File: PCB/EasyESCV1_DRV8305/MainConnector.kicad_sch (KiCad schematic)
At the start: 3 parts, among them J1 10159560-A00221RLF, J2 TC2050-IDC, U4 LMR16006XDDCR

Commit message: Finished REV1 Schematic Awaiting Review
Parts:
- removed J2: TC2050-IDC, Connector:Tag-Connect_TC2050-IDC-NL_2x05_P1.27mm_Vertical, symbol Connectors:TC2050-IDC
- added 3V3: TestPoint, symbol Connector:TestPoint
- added C18: 390U, symbol Device:C_Polarized_US
- added C19: 0.1U, symbol Device:C
- added C20: 0.33u, symbol Device:C
- added C21: 22u, symbol Device:C
- added C22: 1u, symbol Device:C
- added D2: D_Schottky, symbol Device:D_Schottky
- added L1: 15u, symbol Device:L
- added R13: 24.9K, symbol Device:R_US
- added R14: 4.99K, symbol Device:R_US
- added R15: 68k, symbol Device:R_US
- added R16: 20k, symbol Device:R_US
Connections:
- net PVDD: now reaches J1.1
- net PVDD: now also J1.2, U4.5 (VIN), C18.1, C22.1, R13.1
- net COM: now reaches J1.10
- net GND: now reaches J1.3
- net GND: now also J1.4, J1.8, J1.9, J1.S1 (SHIELD), J1.S2 (SHIELD__1), U4.2 (GND), C18.2, C19.2, C21.2, C22.2, D2.2 (A), R14.2, R16.2
- net MOT_A: now reaches J1.5
- net MOT_B: now reaches J1.6
- net MOT_C: now reaches J1.7
- net at U4.1 (CB): now also C20.2
- net at U4.3 (FB): now also R15.2, R16.1
- net at U4.6 (SW): now also C20.1, D2.1 (K), L1.1
- new net 3.3V: 3V3.1, C21.1, L1.2, R15.1
- new net VSEN_PVDD: C19.1, R13.2, R14.1
- no-connect marks 0 -> 1
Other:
- note added: "3V3 Buck Regulator"
- note added: "Input Power"
- note added: "Main Connector"
- company: (none) -> Buckley Boards 
- title: (none) -> Easy ESC
- moved on the sheet: J1, U4

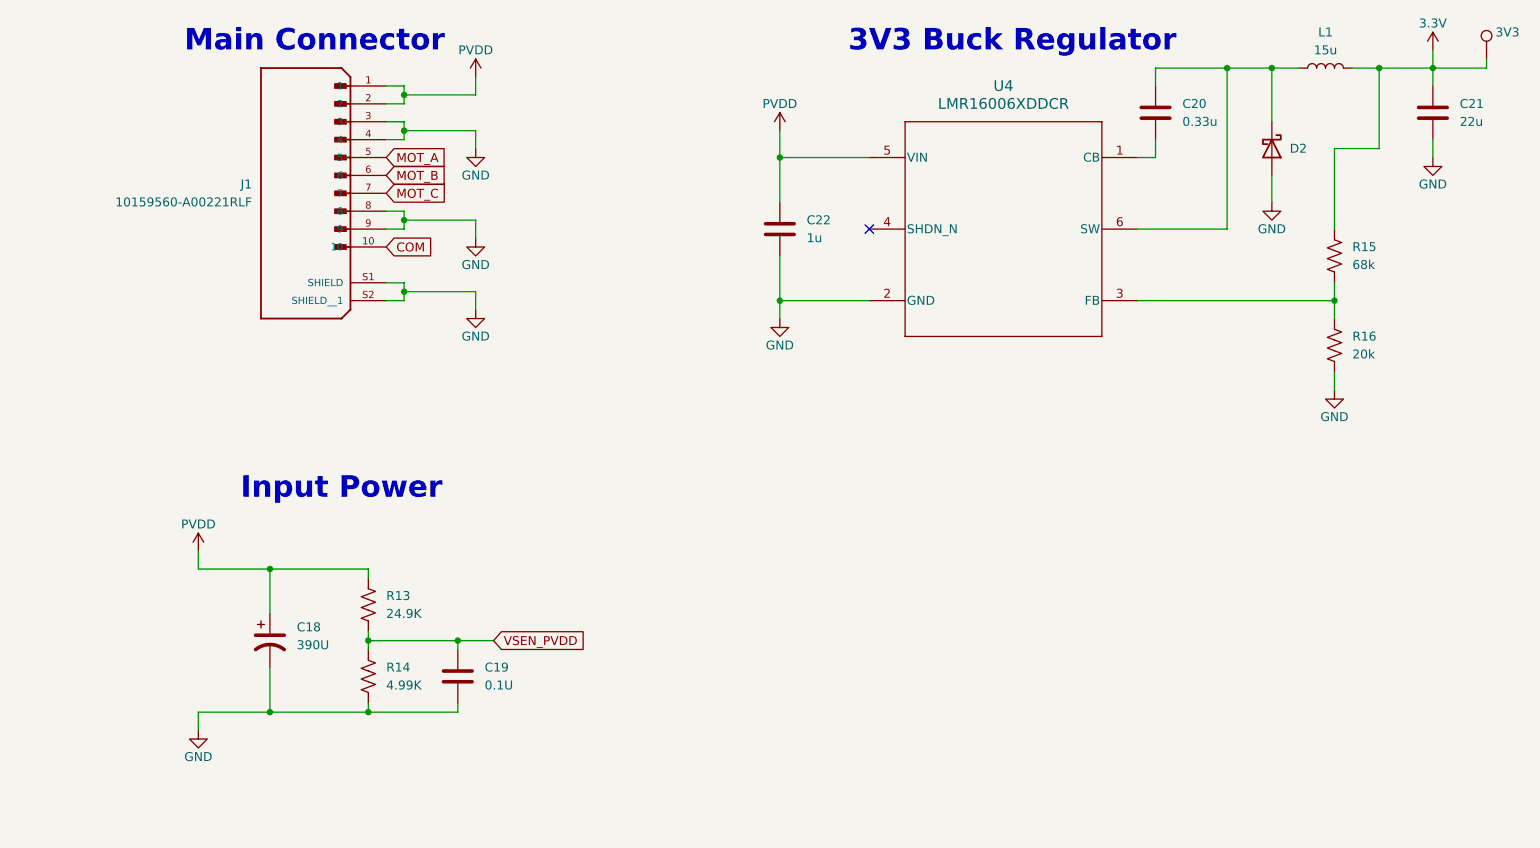
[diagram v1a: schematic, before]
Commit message: Fixed issue with fet symbol and started layout
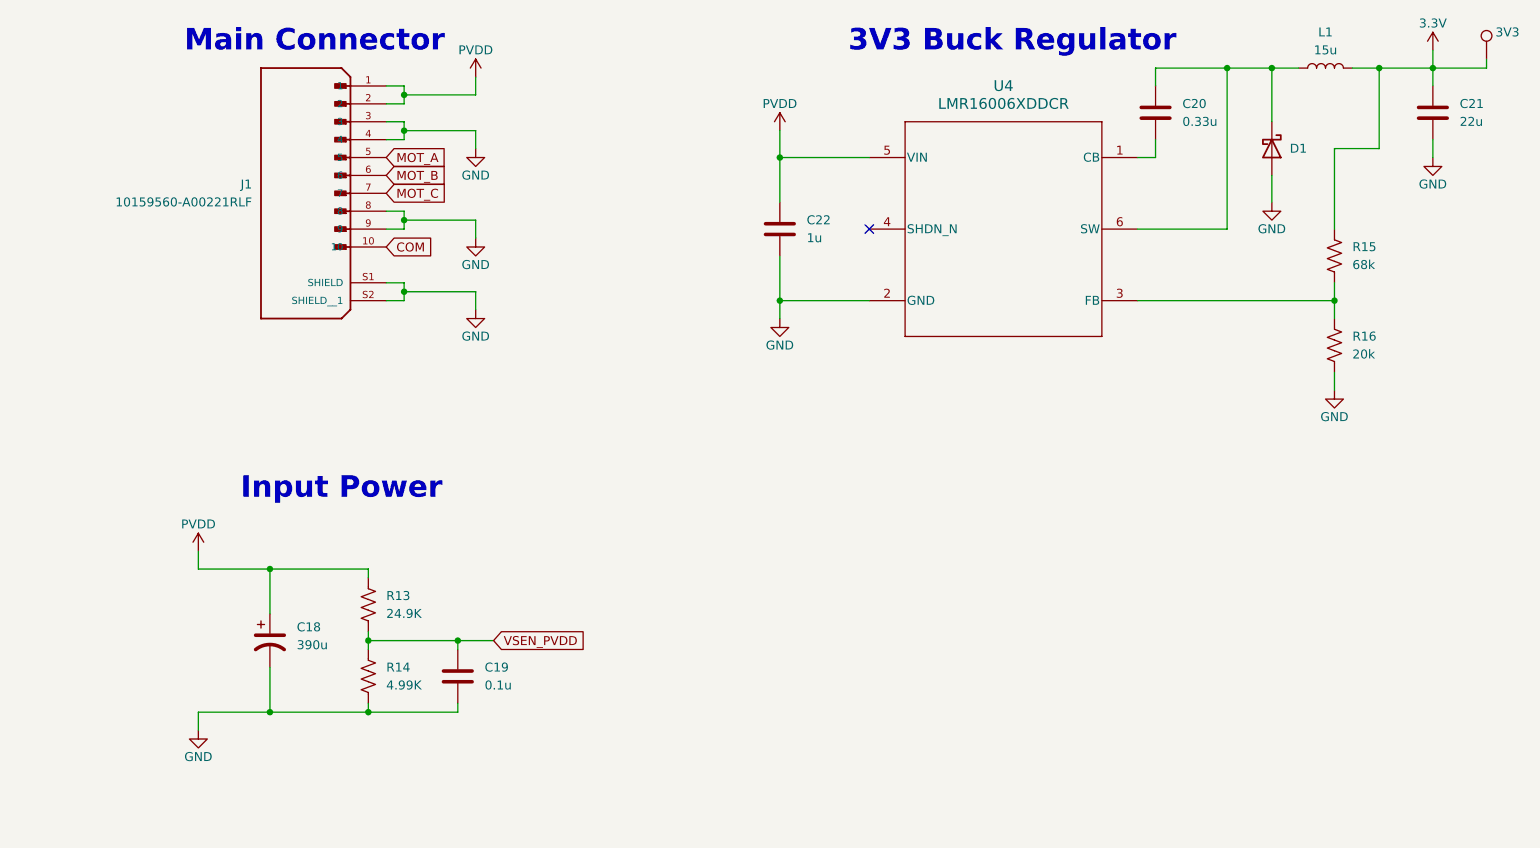
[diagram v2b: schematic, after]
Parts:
- 3V3: footprint (none) -> TestPoint:TestPoint_Pad_D3.0mm
- C18: value 390U -> 390u
- C19: value 0.1U -> 0.1u; footprint (none) -> Capacitor_SMD:C_0402_1005Metric
- C20, C21, C22: footprint (none) -> Capacitor_SMD:C_0603_1608Metric
- D1: renamed from D2; footprint (none) -> Diode_SMD:D_SOD-123
- J1: footprint 10159560-A00221RLF:AMPHENOL_10159560-A00221RLF -> Connectors:AMPHENOL_10159560-A00221RLF
- R13, R15, R16: footprint (none) -> Resistor_SMD:R_0603_1608Metric
- R14: footprint (none) -> Resistor_SMD:R_0402_1005Metric
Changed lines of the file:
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@@
 			)
 		)
-		(property "Value" "390U"
+		(property "Value" "390u"
 			(at 63.5 127.6349 0)
 			(effects
@@
 			)
 		)
-		(property "Footprint" ""
+		(property "Footprint" "Capacitor_SMD:C_0603_1608Metric"
 			(at 133.0452 72.39 0)
 			(effects
@@
 			)
 		)
-		(property "Footprint" "10159560-A00221RLF:AMPHENOL_10159560-A00221RLF"
+		(property "Footprint" "Connectors:AMPHENOL_10159560-A00221RLF"
 			(at 71.12 60.96 0)
 			(effects
@@
 			)
 		)
-		(property "Footprint" ""
+		(property "Footprint" "TestPoint:TestPoint_Pad_D3.0mm"
 			(at 237.49 44.45 0)
 			(effects
@@
 		(on_board yes)
 		(dnp no)
-		(property "Reference" "D2"
+		(property "Reference" "D1"
 			(at 204.47 57.15 90)
 			(effects
@@
 			)
 		)
-		(property "Footprint" ""
+		(property "Footprint" "Diode_SMD:D_SOD-123"
 			(at 201.93 57.15 0)
 			(effects
@@
 			(project ""
 				(path "/6c304649-7c80-4a4c-b925-07b9210ad53d/22fb4715-9f33-45f1-b8d4-9537d945fe69"
-					(reference "D2")
+					(reference "D1")
 					(unit 1)
 				)
@@
 			)
 		)
-		(property "Value" "0.1U"
+		(property "Value" "0.1u"
 			(at 90.17 133.3499 0)
 			(effects
@@
 			)
 		)
-		(property "Footprint" ""
+		(property "Footprint" "Capacitor_SMD:C_0402_1005Metric"
 			(at 87.3252 135.89 0)
 			(effects
@@
 			)
 		)
-		(property "Footprint" ""
+		(property "Footprint" "Resistor_SMD:R_0603_1608Metric"
 			(at 211.836 85.344 90)
 			(effects
@@
 			)
 		)
-		(property "Footprint" ""
+		(property "Footprint" "Resistor_SMD:R_0402_1005Metric"
 			(at 74.676 132.334 90)
 			(effects
@@
 			)
 		)
-		(property "Footprint" ""
+		(property "Footprint" "Capacitor_SMD:C_0603_1608Metric"
 			(at 186.3852 55.88 0)
 			(effects
@@
 			)
 		)
-		(property "Footprint" ""
+		(property "Footprint" "Resistor_SMD:R_0603_1608Metric"
 			(at 211.836 72.644 90)
 			(effects
@@
 			)
 		)
-		(property "Footprint" ""
+		(property "Footprint" "Resistor_SMD:R_0603_1608Metric"
 			(at 74.676 122.174 90)
 			(effects
@@
 			)
 		)
-		(property "Footprint" ""
+		(property "Footprint" "Capacitor_SMD:C_0603_1608Metric"
 			(at 225.7552 55.88 0)
 			(effects
